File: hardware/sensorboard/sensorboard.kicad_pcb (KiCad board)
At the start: 2 copper layers, 51.7 x 19.1 mm, 23 parts, among them P1 PWR, P2 PROG, U1 ESP-07v2, U2 LMR16006Y, U3 BMP180_board, U4 DHT22

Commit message: Bro do you even switch
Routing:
- net +3V3: track 73.8 -> 109.8 mm, vias 3 -> 8
- net GND: track 13.7 -> 18.7 mm, vias 3 -> 7
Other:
- net class 3v3 added: clearance 0.2, trace_width 0.5, via_dia 1, via_drill 0.6
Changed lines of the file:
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@@
     (links 51)
     (no_connects 0)
-    (area 123.324999 72.314999 175.208001 91.775001)
+    (area 123.324999 72.314999 175.208001 91.575001)
     (thickness 1.6)
     (drawings 20)
-    (tracks 130)
+    (tracks 157)
     (zones 0)
     (modules 23)
@@
     (uvia_drill 0.1)
     (add_net +3.3VP)
-    (add_net +3V3)
     (add_net +6V)
     (add_net ADC_IN)
@@
     (add_net RXD)
     (add_net TXD)
+  )
+  (net_class 3v3 ""
+    (clearance 0.2)
+    (trace_width 0.5)
+    (via_dia 1)
+    (via_drill 0.6)
+    (uvia_dia 0.3)
+    (uvia_drill 0.1)
+    (add_net +3V3)
   )
   (module Capacitors_SMD:C_0805_HandSoldering (layer F.Cu)
@@
     (descr "6-pin SOT-23 package")
     (tags SOT-23-6)
+    (solder_mask_margin 0.1)
     (attr smd)
     (fp_text reference U2 (at 1.025 -0.075 450) (layer F.SilkS)
@@
   (gr_line (start 175.133 72.39) (end 175.133 72.517) (angle 90) (layer Edge.Cuts) (width 0.15))
   (gr_line (start 128.27 72.39) (end 175.133 72.39) (angle 90) (layer Edge.Cuts) (width 0.15))
-  (segment (start 135.075 75.975) (end 135.375 75.975) (width 0.25) (layer F.Cu) (net 0))
   (segment (start 128 74.5) (end 131.3 74.5) (width 0.25) (layer F.Cu) (net 1))
   (segment (start 131.3 74.5) (end 131.4 74.4) (width 0.25) (layer F.Cu) (net 1))
@@
   (segment (start 130.375 78.625) (end 130.875 79.125) (width 0.25) (layer F.Cu) (net 1))
   (segment (start 128 74.5) (end 128.5 74.5) (width 0.25) (layer F.Cu) (net 1))
+  (segment (start 124.6 83.6) (end 125.6 83.6) (width 0.25) (layer F.Cu) (net 2))
+  (segment (start 126.075 83.125) (end 126.875 83.125) (width 0.25) (layer F.Cu) (net 2) (status 800000))
+  (segment (start 125.6 83.6) (end 126.075 83.125) (width 0.25) (layer F.Cu) (net 2))
+  (via (at 125.6 83.6) (size 0.6) (drill 0.4) (layers F.Cu B.Cu) (net 2))
+  (via (at 124.6 83.6) (size 0.6) (drill 0.4) (layers F.Cu B.Cu) (net 2))
+  (segment (start 124.6 82.5) (end 125.6 82.5) (width 0.25) (layer F.Cu) (net 2))
+  (via (at 125.6 82.5) (size 0.6) (drill 0.4) (layers F.Cu B.Cu) (net 2))
+  (segment (start 125.6 82.5) (end 126.325 83.125) (width 0.25) (layer F.Cu) (net 2))
+  (via (at 124.6 82.5) (size 0.6) (drill 0.4) (layers F.Cu B.Cu) (net 2))
+  (segment (start 126.875 83.125) (end 126.325 83.125) (width 0.25) (layer F.Cu) (net 2) (status C00000))
   (via (at 144.75 87.55) (size 0.6) (drill 0.4) (layers F.Cu B.Cu) (net 2))
   (segment (start 144.75 87.55) (end 144.7 87.6) (width 0.25) (layer B.Cu) (net 2))
@@
   (segment (start 135.175 79.125) (end 135.9 78.4) (width 0.25) (layer F.Cu) (net 2))
   (segment (start 134.225 79.125) (end 134.625 79.125) (width 0.25) (layer F.Cu) (net 2))
+  (segment (start 126.875 85.625) (end 125.875 85.625) (width 0.5) (layer F.Cu) (net 3))
+  (segment (start 124.2 87.3) (end 124.6 86.9) (width 0.25) (layer B.Cu) (net 3))
+  (via (at 124.6 86.9) (size 1) (drill 0.6) (layers F.Cu B.Cu) (net 3))
+  (segment (start 124.2 87.3) (end 124.1 87.3) (width 0.25) (layer B.Cu) (net 3))
+  (segment (start 125.875 85.625) (end 124.6 86.9) (width 0.5) (layer F.Cu) (net 3))
+  (segment (start 126.875 85.625) (end 124.775 85.625) (width 0.5) (layer F.Cu) (net 3))
+  (segment (start 124.775 85.625) (end 124.6 85.8) (width 0.5) (layer F.Cu) (net 3))
+  (via (at 142.3 89.3) (size 0.6) (drill 0.4) (layers F.Cu B.Cu) (net 3))
+  (segment (start 142.3 76) (end 142.3 89.3) (width 0.25) (layer F.Cu) (net 3))
+  (segment (start 142.45 89.45) (end 144.75 89.45) (width 0.25) (layer B.Cu) (net 3))
+  (segment (start 142.3 89.3) (end 142.45 89.45) (width 0.25) (layer B.Cu) (net 3))
+  (via (at 133.3 74.4) (size 0.6) (drill 0.4) (layers F.Cu B.Cu) (net 3))
+  (segment (start 133.3 74.4) (end 131.9 73) (width 0.25) (layer B.Cu) (net 3))
+  (segment (start 131.9 73) (end 124.5 73) (width 0.25) (layer B.Cu) (net 3))
+  (segment (start 124.5 73) (end 123.8 73.7) (width 0.25) (layer B.Cu) (net 3))
+  (segment (start 123.8 73.7) (end 123.8 85) (width 0.25) (layer B.Cu) (net 3))
+  (segment (start 123.8 85) (end 124.6 85.8) (width 0.25) (layer B.Cu) (net 3))
+  (via (at 124.6 85.8) (size 1) (drill 0.6) (layers F.Cu B.Cu) (net 3))
+  (segment (start 124.6 85.8) (end 124.775 85.625) (width 0.25) (layer F.Cu) (net 3))
+  (segment (start 133.3 74) (end 133.3 74.4) (width 0.25) (layer F.Cu) (net 3))
+  (via (at 144.75 89.45) (size 0.6) (drill 0.4) (layers F.Cu B.Cu) (net 3))
+  (segment (start 148.5011 88.5236) (end 147.5747 89.45) (width 0.5) (layer F.Cu) (net 3))
+  (segment (start 144.75 89.45) (end 147.5747 89.45) (width 0.5) (layer F.Cu) (net 3))
+  (segment (start 124.1 89.7) (end 124.1 87.3) (width 0.5) (layer B.Cu) (net 3))
+  (segment (start 125.4 91) (end 124.1 89.7) (width 0.5) (layer B.Cu) (net 3))
+  (segment (start 143.2 91) (end 125.4 91) (width 0.5) (layer B.Cu) (net 3))
+  (segment (start 144.75 89.45) (end 143.2 91) (width 0.5) (layer B.Cu) (net 3))
+  (segment (start 124.1 87.3) (end 124.1 87.2) (width 0.25) (layer B.Cu) (net 3))
   (segment (start 166.116 84.666) (end 166.116 84.484) (width 0.25) (layer F.Cu) (net 3))
   (segment (start 166.116 84.484) (end 167.6 83) (width 0.25) (layer F.Cu) (net 3))
@@
   (segment (start 149.9 90.9) (end 166.7 90.9) (width 0.25) (layer F.Cu) (net 3))
   (segment (start 148.5011 89.5011) (end 149.9 90.9) (width 0.25) (layer F.Cu) (net 3))
-  (segment (start 142.3 76) (end 142.3 89.3) (width 0.25) (layer F.Cu) (net 3))
   (via (at 142.3 74.4) (size 0.6) (drill 0.4) (layers F.Cu B.Cu) (net 3))
   (via (at 142.3 76) (size 0.6) (drill 0.4) (layers F.Cu B.Cu) (net 3))
   (segment (start 142.3 74.4) (end 142.3 76) (width 0.25) (layer B.Cu) (net 3))
-  (segment (start 133.3 74.4) (end 133.3 74) (width 0.25) (layer F.Cu) (net 3))
-  (segment (start 133.3 74) (end 134.1 73.2) (width 0.25) (layer F.Cu) (net 3))
-  (segment (start 134.1 73.2) (end 135.5 73.2) (width 0.25) (layer F.Cu) (net 3))
-  (segment (start 135.5 73.2) (end 136.4 74.1) (width 0.25) (layer F.Cu) (net 3))
-  (segment (start 136.4 74.1) (end 136.4 79.5) (width 0.25) (layer F.Cu) (net 3))
-  (segment (start 136.4 79.5) (end 137.6 80.7) (width 0.25) (layer F.Cu) (net 3))
-  (segment (start 137.6 80.7) (end 137.6 89.5) (width 0.25) (layer F.Cu) (net 3))
-  (segment (start 144.75 89.45) (end 147.5747 89.45) (width 0.25) (layer F.Cu) (net 3))
-  (segment (start 147.5747 89.45) (end 148.5011 88.5236) (width 0.25) (layer F.Cu) (net 3))
   (via (at 168.656 84.648) (size 0.6) (drill 0.4) (layers F.Cu B.Cu) (net 4))
   (segment (start 172.024 81.28) (end 168.656 84.648) (width 0.25) (layer F.Cu) (net 4))
@@
     (polygon
       (pts
-        (xy 127.75 89) (xy 145.5 88.75) (xy 145.5 91) (xy 123.75 91) (xy 123.75 85)
+        (xy 127.75 89) (xy 136.8 88.85) (xy 136.8 91.1) (xy 123.75 91) (xy 123.75 85)
         (xy 127.75 85) (xy 127.75 89)
       )
@@
     (polygon
       (pts
-        (xy 175 91.4) (xy 123.7 91.2) (xy 123.7 72.8) (xy 175 72.8) (xy 175 91.4)
+        (xy 126.8 72.8) (xy 175 72.8) (xy 175 91.4) (xy 123.7 91.2) (xy 123.7 76.2)
+        (xy 126.8 76.2) (xy 126.8 72.8)
       )
     )

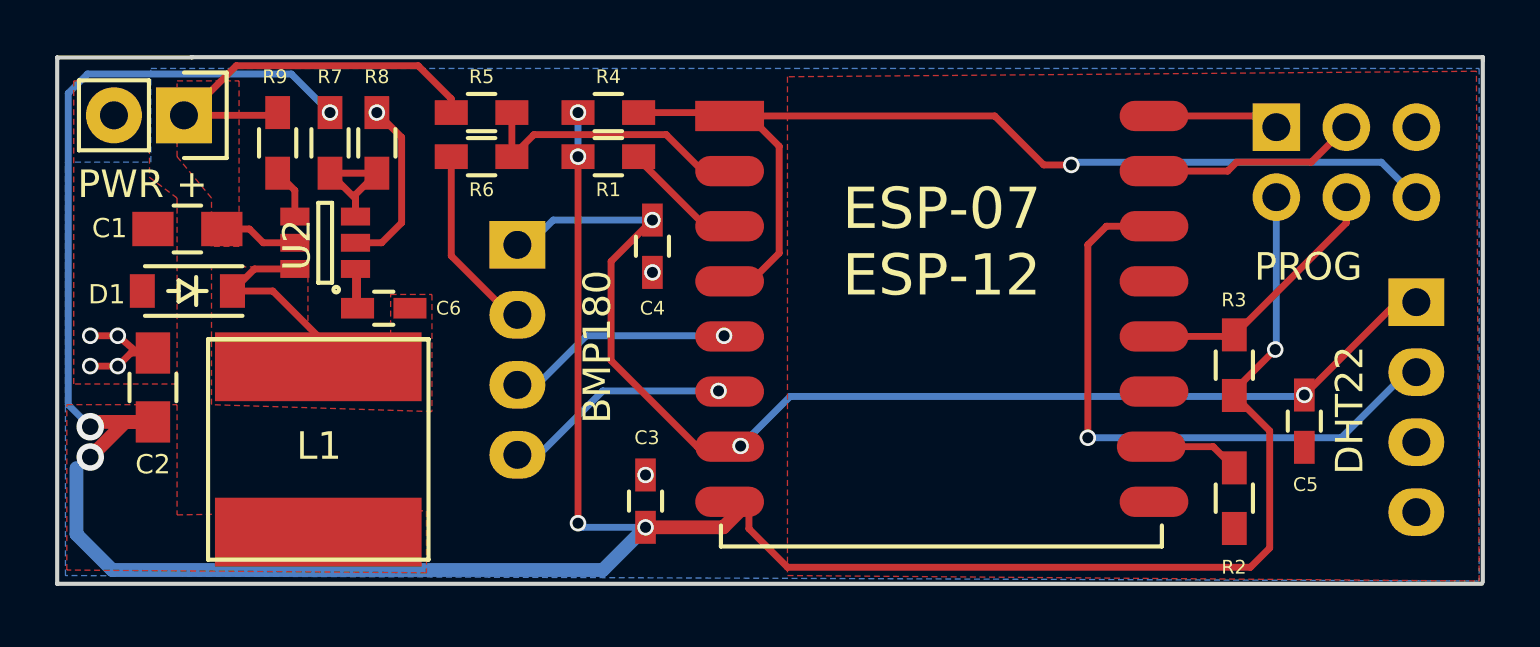
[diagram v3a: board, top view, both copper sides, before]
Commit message: Fix up the 3v3 traces
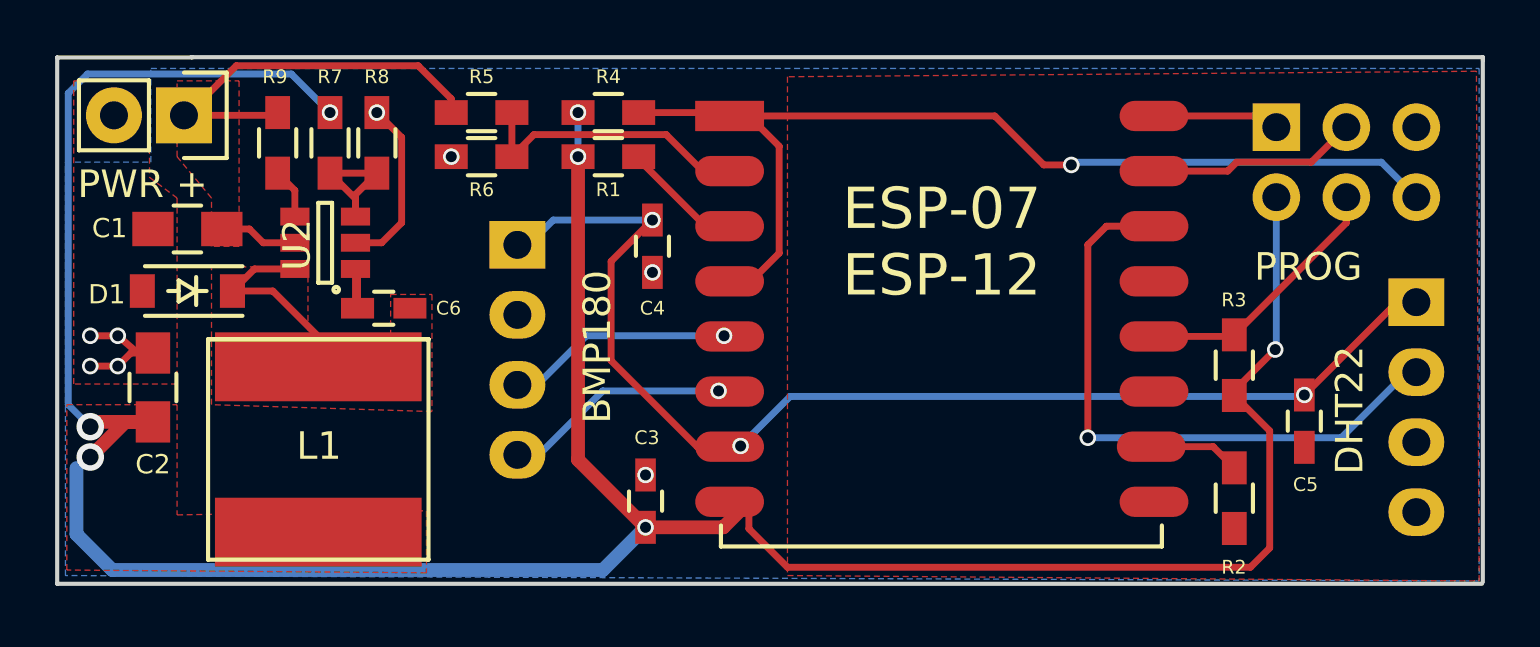
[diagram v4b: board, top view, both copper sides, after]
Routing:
- net GND: track 18.7 -> 12.1 mm, vias 7 -> 8
- net +3V3: track 109.8 -> 108.4 mm, vias 8 -> 7
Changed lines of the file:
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@@
     (links 51)
     (no_connects 0)
-    (area 123.324999 72.314999 175.208001 91.575001)
+    (area 123.324999 65.548599 175.208001 91.575001)
     (thickness 1.6)
     (drawings 20)
-    (tracks 157)
+    (tracks 154)
     (zones 0)
     (modules 23)
@@
   (segment (start 130.375 78.625) (end 130.875 79.125) (width 0.25) (layer F.Cu) (net 1))
   (segment (start 128 74.5) (end 128.5 74.5) (width 0.25) (layer F.Cu) (net 1))
+  (via (at 137.7 76) (size 0.6) (drill 0.4) (layers F.Cu B.Cu) (net 2) (status C00000))
   (segment (start 124.6 83.6) (end 125.6 83.6) (width 0.25) (layer F.Cu) (net 2))
   (segment (start 126.075 83.125) (end 126.875 83.125) (width 0.25) (layer F.Cu) (net 2) (status 800000))
@@
   (segment (start 144.75 87.55) (end 144.7 87.6) (width 0.25) (layer B.Cu) (net 2))
   (via (at 145 80.2) (size 0.6) (drill 0.4) (layers F.Cu B.Cu) (net 2))
-  (segment (start 137.7 76) (end 137.7 79.6) (width 0.25) (layer F.Cu) (net 2))
-  (segment (start 137.7 79.6) (end 139.84 81.74) (width 0.25) (layer F.Cu) (net 2))
   (segment (start 139.84 81.74) (end 140.1 81.74) (width 0.25) (layer F.Cu) (net 2))
   (via (at 135 74.4) (size 0.6) (drill 0.4) (layers F.Cu B.Cu) (net 2))
@@
   (segment (start 135.175 79.125) (end 135.9 78.4) (width 0.25) (layer F.Cu) (net 2))
   (segment (start 134.225 79.125) (end 134.625 79.125) (width 0.25) (layer F.Cu) (net 2))
+  (segment (start 142.3 76) (end 142.3 87) (width 0.5) (layer F.Cu) (net 3) (status 400000))
+  (segment (start 142.3 87) (end 144.75 89.45) (width 0.5) (layer F.Cu) (net 3) (status 800000))
   (segment (start 126.875 85.625) (end 125.875 85.625) (width 0.5) (layer F.Cu) (net 3))
   (segment (start 124.2 87.3) (end 124.6 86.9) (width 0.25) (layer B.Cu) (net 3))
@@
   (segment (start 126.875 85.625) (end 124.775 85.625) (width 0.5) (layer F.Cu) (net 3))
   (segment (start 124.775 85.625) (end 124.6 85.8) (width 0.5) (layer F.Cu) (net 3))
-  (via (at 142.3 89.3) (size 0.6) (drill 0.4) (layers F.Cu B.Cu) (net 3))
-  (segment (start 142.3 76) (end 142.3 89.3) (width 0.25) (layer F.Cu) (net 3))
-  (segment (start 142.45 89.45) (end 144.75 89.45) (width 0.25) (layer B.Cu) (net 3))
-  (segment (start 142.3 89.3) (end 142.45 89.45) (width 0.25) (layer B.Cu) (net 3))
   (via (at 133.3 74.4) (size 0.6) (drill 0.4) (layers F.Cu B.Cu) (net 3))
   (segment (start 133.3 74.4) (end 131.9 73) (width 0.25) (layer B.Cu) (net 3))
@@
   (segment (start 133.3 74) (end 133.3 74.4) (width 0.25) (layer F.Cu) (net 3))
   (via (at 144.75 89.45) (size 0.6) (drill 0.4) (layers F.Cu B.Cu) (net 3))
+  (segment (start 144.75 89.45) (end 143.2 91) (width 0.5) (layer B.Cu) (net 3))
+  (segment (start 143.2 91) (end 125.4 91) (width 0.5) (layer B.Cu) (net 3))
+  (segment (start 125.4 91) (end 124.1 89.7) (width 0.5) (layer B.Cu) (net 3))
+  (segment (start 124.1 89.7) (end 124.1 87.3) (width 0.5) (layer B.Cu) (net 3))
   (segment (start 148.5011 88.5236) (end 147.5747 89.45) (width 0.5) (layer F.Cu) (net 3))
   (segment (start 144.75 89.45) (end 147.5747 89.45) (width 0.5) (layer F.Cu) (net 3))
-  (segment (start 124.1 89.7) (end 124.1 87.3) (width 0.5) (layer B.Cu) (net 3))
-  (segment (start 125.4 91) (end 124.1 89.7) (width 0.5) (layer B.Cu) (net 3))
-  (segment (start 143.2 91) (end 125.4 91) (width 0.5) (layer B.Cu) (net 3))
-  (segment (start 144.75 89.45) (end 143.2 91) (width 0.5) (layer B.Cu) (net 3))
   (segment (start 124.1 87.3) (end 124.1 87.2) (width 0.25) (layer B.Cu) (net 3))
   (segment (start 166.116 84.666) (end 166.116 84.484) (width 0.25) (layer F.Cu) (net 3))
